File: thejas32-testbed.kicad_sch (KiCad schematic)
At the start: 128 parts, among them J1 Conn_02x04_Odd_Even, J10 Conn_02x10_Odd_Even, J11 Conn_02x03_Odd_Even, J13 Conn_02x06_Odd_Even, J15 Conn_01x04, J2 USB_B_Micro, J3 Conn_02x03_Odd_Even, J4 Conn_02x04_Odd_Even, J5 Conn_02x06_Odd_Even, J6 Conn_02x06_Odd_Even, J7 Conn_02x03_Odd_Even, J8 Conn_02x06_Odd_Even, J9 Conn_02x10_Odd_Even, U1 Pico Master, U2 THEJAS32, U3 Pico Slave, U4 MINI360 DC-DC, U5 MINI360 DC-DC, U6 W25Q16JVSSIQ

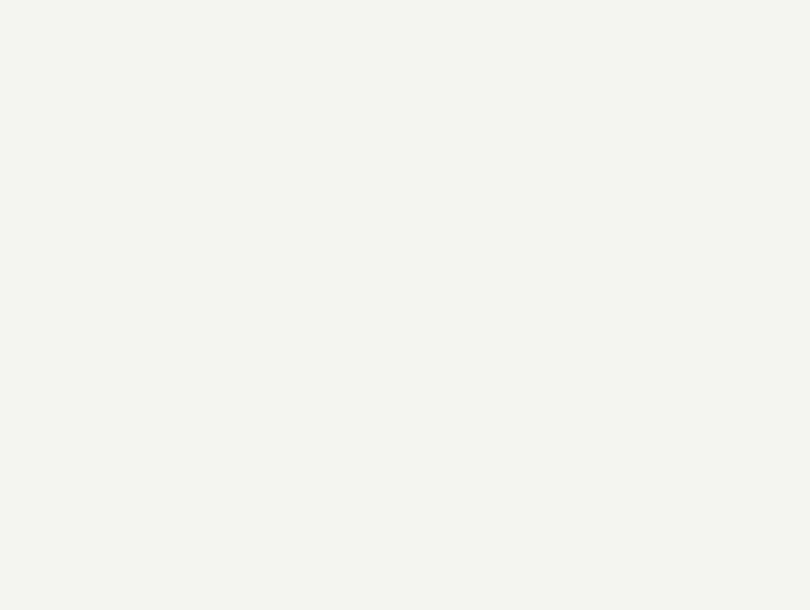
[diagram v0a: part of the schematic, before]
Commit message: Add PTH on board edges
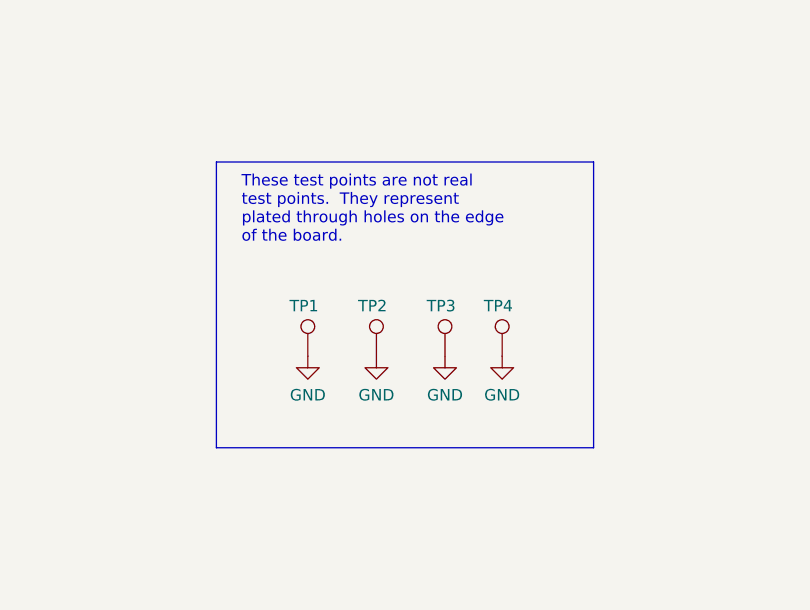
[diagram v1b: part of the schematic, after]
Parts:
- added TP1, TP2, TP3, TP4: Mounting Hole, MountingHole:MountingHole_3.2mm_M3_Pad, symbol Connector:TestPoint
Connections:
- net GND: now also TP1.1, TP2.1, TP3.1, TP4.1
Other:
- note added: "These test points are not real test points. They represent plated through holes on the edge of the board."

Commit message: Add footprint for Mini360
Roughly tested using calipers against a physical module.

Source of footprint:

https://github.com/rayvburn/KiCad/tree/master/Mini360_step_down_converter/Mini360_step-down.pretty

Commit 69583e8
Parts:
- U4, U5: footprint Module_DCDC:Mini 360 -> project_lib:Mini360_step-down
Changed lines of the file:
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@@
 			)
 		)
-		(property "Footprint" "Module_DCDC:Mini 360"
+		(property "Footprint" "project_lib:Mini360_step-down"
 			(at 252.73 128.27 0)
 			(effects
@@
 			)
 		)
-		(property "Footprint" "Module_DCDC:Mini 360"
+		(property "Footprint" "project_lib:Mini360_step-down"
 			(at 252.73 95.25 0)
 			(effects

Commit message: Various simplifications, initial routing.
This is a commit for review.

Schematic is modified to remove many zero ohms. RPi
connector brought in.

Layout shows 3V3 and 1V2 power planes. Pin mapping
may need to change to avoid usage of layer 3 for
signals if possible.
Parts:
- removed J15: Conn_01x04, Connector_PinHeader_2.54mm:PinHeader_1x04_P2.54mm_Vertical, symbol Connector_Generic:Conn_01x04
- removed J5, J8: Conn_02x06_Odd_Even, Connector_PinHeader_2.54mm:PinHeader_2x06_P2.54mm_Vertical, symbol Connector_Generic:Conn_02x06_Odd_Even
- removed J7: Conn_02x03_Odd_Even, Connector_PinHeader_2.54mm:PinHeader_2x03_P2.54mm_Vertical, symbol Connector_Generic:Conn_02x03_Odd_Even
- removed J9: Conn_02x10_Odd_Even, Connector_PinHeader_2.54mm:PinHeader_2x10_P2.54mm_Vertical, symbol Connector_Generic:Conn_02x10_Odd_Even
- removed R17, R19, R21, R23, R44, R45, R46, R47, R48, R49, R50, R51, R52, R53, R54, R55, R56, R57, R58, R59, R60, R61, R62, R63, R64, R65, R66, R67, R68, R69, R71: 0E, project_lib:proj_R_0603_1608Metric_Pad0.98x0.95mm_HandSolder, symbol Project-Specific:R_HandSolderable
- removed U4, U5: MINI360 DC-DC, project_lib:Mini360_step-down, symbol Mini360_Buck_Module:Mini360
- added J12: Conn_02x20_Odd_Even, Connector_PinHeader_2.54mm:PinHeader_2x20_P2.54mm_Vertical, symbol Connector_Generic:Conn_02x20_Odd_Even
- added J7: Conn_01x06, Connector_PinHeader_2.54mm:PinHeader_1x06_P2.54mm_Vertical, symbol Connector_Generic:Conn_01x06
- added JP1, JP2, JP3, JP4: Jumper_2_Bridged, Connector_PinHeader_2.54mm:PinHeader_1x02_P2.54mm_Vertical, symbol Jumper:Jumper_2_Bridged
- added U4, U5: ~, project_lib:Mini360_step-down, symbol Project-Specific:MINI360_DC-DC
- R38, R39, R40, R41, R42, R43: value 0E -> 10K
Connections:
- net +3V3 is gone; now on net PWR_3V3: C25.1, C25A1.1, J10.1 (Pin_1), J10.2 (Pin_2), J13.1 (Pin_1), J13.2 (Pin_2), J6.1 (Pin_1), J6.2 (Pin_2), U6.8 (VCC)
- net MCU_GPIO_02 is gone; now on net MCU_TST_CLK: R38.2
- net MCU_GPIO_03 is gone; now on net MCU_TJTAG_TMS: R39.2
- net MCU_GPIO_04 is gone; now on net MCU_TJTAG_TDI: R40.2
- net MCU_GPIO_05 is gone; now on net MCU_TJTAG_TCK: R41.2
- net MCU_GPIO_06 is gone; now on net MCU_TJTAG_TRST: R42.2
- net MCU_GPIO_07 is gone; now on net MCU_TST_MODE: R43.2
- net GND: now also R38.1, R39.1, R40.1, R41.1, R42.1, R43.1, J12.14 (Pin_14), J12.20 (Pin_20), J12.25 (Pin_25), J12.30 (Pin_30), J12.34 (Pin_34), J12.39 (Pin_39), J12.6 (Pin_6), J12.9 (Pin_9), J7.6 (Pin_6), U4.1 (IN-), U4.3 (OUT-), U5.1 (IN-), U5.3 (OUT-)
- net MCU_GPIO_16: now also U2.6 (GPIO16)
- net MCU_GPIO_17: now also U2.5 (GPIO17)
- net MCU_GPIO_18: now also U2.2 (GPIO18)
- net MCU_GPIO_19: now also U2.1 (GPIO19)
- net MCU_GPIO_20: now also U2.128 (GPIO20)
- net MCU_GPIO_21: now also U2.127 (GPIO21)
- net MCU_GPIO_22: now also U2.122 (GPIO22)
- net MCU_GPIO_23: now also U2.121 (GPIO23)
- net MCU_GPIO_24: now also U2.120 (GPIO24)
- net MCU_GPIO_25: now also U2.119 (GPIO25)
- net MCU_GPIO_26: now also U2.118 (GPIO26)
- net MCU_GPIO_27: now also U2.117 (GPIO27)
- net MCU_GPIO_28: now also U2.116 (GPIO28)
- net MCU_GPIO_29: now also U2.111 (GPIO29)
- net MCU_GPIO_30: now also U2.110 (GPIO30)
- net MCU_GPIO_31: now also U2.109 (GPIO31)
- net MCU_PWM_4: now also J7.2 (Pin_2)
- net MCU_PWM_5: now also J7.3 (Pin_3)
- net MCU_PWM_6: now also J7.4 (Pin_4)
- net MCU_PWM_7: now also J7.5 (Pin_5)
- net MCU_UART1_RX: now also U3.6 (GPIO4)
- net MCU_UART1_TX: now also U3.7 (GPIO5)
- net PWR_1V2: now also JP2.2 (B)
- net PWR_3V3: now also J12.1 (Pin_1), J12.17 (Pin_17), J7.1 (Pin_1), JP1.2 (B)
- net RPi_COMPAT_UART_TXD: now reaches R14.2
- net RPi_COMPAT_UART_TXD: now also J12.8 (Pin_8)
- net RPi_COMPAT_UART_RXD: now reaches R15.2
- net RPi_COMPAT_UART_RXD: now also J12.10 (Pin_10)
- net RPi_COMPAT_GPIO_7: now reaches U2.55 (GPIO11)
- net RPi_COMPAT_GPIO_7: now also J12.26 (Pin_26)
- net at U2.10 (SPI3_MISO): now also U6.2 (DO(IO1))
- net at U2.12 (SPI3_SS): now also U6.1 (~{CS})
- net MCU_TST_CLK: now reaches U2.20 (TST_CLK)
- net MCU_TJTAG_TMS: now reaches U2.22 (TJTAG_TMS)
- net MCU_TJTAG_TDI: now reaches U2.23 (TJTAG_TDI)
- net MCU_TJTAG_TCK: now reaches U2.28 (TJTAG_TCK)
- net MCU_TJTAG_TRST: now reaches U2.29 (TJTAG_TRST)
- net MCU_TST_MODE: now reaches U2.30 (TST_MODE)
- net RPi_COMPAT_I2C1_SCL: now reaches R4.2, U2.33 (I2C0_SCL)
- net RPi_COMPAT_I2C1_SCL: now also J12.5 (Pin_5)
- net RPi_COMPAT_I2C1_SDA: now reaches R5.2, U2.34 (I2C0_SDA)
- net RPi_COMPAT_I2C1_SDA: now also J12.3 (Pin_3)
- net at U2.39 (SPI1_SS): now also J13.5 (Pin_5)
- net at U2.41 (SPI1_MISO): now also J13.9 (Pin_9)
- net RPi_COMPAT_GPIO_21: now reaches U2.51 (GPIO15)
- net RPi_COMPAT_GPIO_21: now also J12.40 (Pin_40)
- net RPi_COMPAT_GPIO_20: now reaches U2.52 (GPIO14)
- net RPi_COMPAT_GPIO_20: now also J12.38 (Pin_38)
- net RPi_COMPAT_GPIO_16: now reaches U2.53 (GPIO13)
- net RPi_COMPAT_GPIO_16: now also J12.36 (Pin_36)
- net RPi_COMPAT_GPIO_1: now reaches U2.54 (GPIO12)
- net RPi_COMPAT_GPIO_1: now also J12.28 (Pin_28)
- net RPi_COMPAT_GPIO_25: now reaches U2.58 (GPIO10)
- net RPi_COMPAT_GPIO_25: now also J12.22 (Pin_22)
- net RPi_COMPAT_GPIO_24: now reaches U2.61 (GPIO9)
- net RPi_COMPAT_GPIO_24: now also J12.18 (Pin_18)
- net RPi_COMPAT_GPIO_23: now reaches U2.62 (GPIO8)
- net RPi_COMPAT_GPIO_23: now also J12.16 (Pin_16)
- net RPi_COMPAT_GPIO_4: now reaches U2.63 (GPIO7)
- net RPi_COMPAT_GPIO_4: now also J12.7 (Pin_7); no longer R43.1
- net RPi_COMPAT_GPIO_17: now reaches U2.64 (GPIO6)
- net RPi_COMPAT_GPIO_17: now also J12.11 (Pin_11); no longer R42.1
- net RPi_COMPAT_GPIO_27: now reaches U2.65 (GPIO5)
- net RPi_COMPAT_GPIO_27: now also J12.13 (Pin_13); no longer R41.1
- net RPi_COMPAT_GPIO_22: now reaches U2.66 (GPIO4)
- net RPi_COMPAT_GPIO_22: now also J12.15 (Pin_15); no longer R40.1
- net at U2.7 (SPI3_MOSI): now also U6.5 (DI(IO0))
- net RPi_COMPAT_GPIO_0: now reaches U2.71 (GPIO3)
- net RPi_COMPAT_GPIO_0: now also J12.27 (Pin_27); no longer R39.1
- net RPi_COMPAT_GPIO_5: now reaches U2.72 (GPIO2)
- net RPi_COMPAT_GPIO_5: now also J12.29 (Pin_29); no longer R38.1
- net RPi_COMPAT_SPI0_MISO: now reaches U2.90 (SPI0_MISO)
- net RPi_COMPAT_SPI0_MISO: now also J12.21 (Pin_21)
- net RPi_COMPAT_SPI0_CE0: now reaches U2.92 (SPI0_CSN)
- net RPi_COMPAT_SPI0_CE0: now also J12.24 (Pin_24)
- net PWR_5V: now reaches J2.1 (VBUS)
- net PWR_5V: now also J12.2 (Pin_2), J12.4 (Pin_4), JP3.1 (A), JP4.1 (A), U4.2 (IN+), U5.2 (IN+)
- net RPi_COMPAT_SPI0_MOSI: now reaches R18.2
- net RPi_COMPAT_SPI0_MOSI: now also J12.19 (Pin_19)
- net at U1.40 (VBUS): now also JP3.2 (B)
- net at U3.40 (VBUS): now also JP4.2 (B)
- net RPi_COMPAT_SPI0_SCLK: now reaches R16.2
- net RPi_COMPAT_SPI0_SCLK: now also J12.23 (Pin_23)
- net MCU_GPIO_00: no longer names the net of U1.4 (GPIO2)
- net MCU_GPIO_00: no longer R36.2
- net MCU_GPIO_01: no longer names the net of U1.5 (GPIO3)
- net MCU_GPIO_01: no longer R37.2
- net MCU_PWM_0 renamed RPi_COMPAT_PWM1
- net RPi_COMPAT_PWM1: now also J12.33 (Pin_33)
- net MCU_PWM_1 renamed RPi_COMPAT_PWM1_ALT
- net RPi_COMPAT_PWM1_ALT: now also J12.35 (Pin_35)
- net MCU_PWM_2 renamed RPi_COMPAT_PWM0
- net RPi_COMPAT_PWM0: now also J12.12 (Pin_12)
- net MCU_PWM_3 renamed RPi_COMPAT_PWM0_ALT
- net RPi_COMPAT_PWM0_ALT: now also J12.32 (Pin_32)
- new net: JP2.1 (A), U5.4 (OUT+)
- new net: JP1.1 (A), U4.4 (OUT+)
- new net RPi_COMPAT_GPIO_26: J12.37 (Pin_37), R36.2
- new net RPi_COMPAT_GPIO_6: J12.31 (Pin_31), R37.2
- no-connect marks 0 -> 48
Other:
- note added: "I2C0 is available on RPI header"
- note added: "Measure 1V2 power consumption in series here."
- note added: "Measure 3V3 power consumption in series here."
- note added: "PWR_FLAG eliminates false ERC errors due to jumpers"
- note added: "Populate this jumper to get power from main connector. Has benefits, including powering RP2040 for USB host."
- note added: "Populate this to get power from main connector. Has benefits, including powering RP2040 for USB host."
- note added: "Raspberry Pi Compatibility Header This header is to help plug common hats and get them to work. From a pinmux and functionality perspective, thejas32 doesn't match the RPi so it's a no-brainer that you should expect only some useful compatibility. Bear in mind that thejas pins have single functionality. E.g. UART pins can't be used as GPIOs... The following are ensured: 3.3V, 5V for appropriately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"
- note added: "SPI0 is available on RPI header"
- note added: "UART2 goes to RPi Connector"
- note removed: "GPIO Header 2"
- note removed: "I2C0 can be tapped here"
- moved on the sheet: C1, C1A1, C2, C2A1, C3, C3A1

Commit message: Review,power shapes,dcap placement from Atharva
All dcaps are now at layer 4, leaving lot
more space on layer 1 for signal breakout.

Flow of 1V2 power is deemed good - power plane,
flowing to caps, through via to pins. Flow of 3V3
power is reasonable - power plane with vias to both
caps and pins.

Connectors and component placements need to be
finalized next, and routed.
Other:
- note added: "Aligned Mounting holes"
- note added: "Change R2 to 100k for weak PD"
- note added: "Change R3 to 100k for weak PD"
- note added: "DEbug UART 0 for master Pico is not conneted anywhere"
- note added: "Need to add Properties like MPN Manufacturer in properties for easier BOM creation"
- note added: "Need to check of R4/R5 has any PU for I2C on Main RasPi. If there, remove R4/R5"
- note added: "When Powering through RasPi, remove JP1"
- moved on the sheet: C11A1
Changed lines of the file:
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@@
 	)
 	(junction
-		(at 314.96 240.03)
-		(diameter 0)
-		(color 0 0 0 0)
-	)
-	(junction
 		(at 175.26 349.25)
 		(diameter 0)
@@
 	)
 	(junction
-		(at 325.12 240.03)
-		(diameter 0)
-		(color 0 0 0 0)
-	)
-	(junction
 		(at 233.68 233.68)
 		(diameter 0)
@@
 	)
 	(junction
-		(at 304.8 240.03)
-		(diameter 0)
-		(color 0 0 0 0)
-	)
-	(junction
 		(at 368.3 393.7)
 		(diameter 0)
@@
 	)
 	(junction
-		(at 335.28 240.03)
-		(diameter 0)
-		(color 0 0 0 0)
-	)
-	(junction
 		(at 58.42 220.98)
 		(diameter 0)
@@
 	)
 	(junction
-		(at 295.91 240.03)
-		(diameter 0)
-		(color 0 0 0 0)
-	)
-	(junction
 		(at 304.8 229.87)
 		(diameter 0)
@@
 	)
 	(junction
-		(at 285.75 240.03)
-		(diameter 0)
-		(color 0 0 0 0)
-	)
-	(junction
 		(at 273.05 284.48)
 		(diameter 0)
@@
 	(wire
 		(pts
-			(xy 314.96 237.49) (xy 314.96 240.03)
+			(xy 314.96 238.76) (xy 314.96 240.03)
 		)
 		(stroke
@@
 	(wire
 		(pts
+			(xy 314.96 231.14) (xy 314.96 229.87)
+		)
+		(stroke
+			(width 0)
+			(type default)
+		)
+	)
+	(wire
+		(pts
 			(xy 74.93 281.94) (xy 149.86 281.94)
 		)
@@
 	(wire
 		(pts
-			(xy 285.75 240.03) (xy 285.75 241.3)
-		)
-		(stroke
-			(width 0)
-			(type default)
-		)
-	)
-	(wire
-		(pts
 			(xy 755.65 424.18) (xy 755.65 440.69)
 		)
@@
 	(wire
 		(pts
-			(xy 335.28 240.03) (xy 335.28 241.3)
-		)
-		(stroke
-			(width 0)
-			(type default)
-		)
-	)
-	(wire
-		(pts
 			(xy 99.06 349.25) (xy 99.06 351.79)
 		)
@@
 	(wire
 		(pts
-			(xy 304.8 240.03) (xy 304.8 241.3)
-		)
-		(stroke
-			(width 0)
-			(type default)
-		)
-	)
-	(wire
-		(pts
 			(xy 130.81 309.88) (xy 149.86 309.88)
 		)
@@
 	(wire
 		(pts
-			(xy 314.96 240.03) (xy 314.96 241.3)
-		)
-		(stroke
-			(width 0)
-			(type default)
-		)
-	)
-	(wire
-		(pts
 			(xy 701.04 473.71) (xy 701.04 486.41)
 		)
@@
 	(wire
 		(pts
-			(xy 295.91 240.03) (xy 295.91 241.3)
-		)
-		(stroke
-			(width 0)
-			(type default)
-		)
-	)
-	(wire
-		(pts
 			(xy 444.5 337.82) (xy 453.39 337.82)
 		)
@@
 	(wire
 		(pts
-			(xy 325.12 240.03) (xy 325.12 241.3)
-		)
-		(stroke
-			(width 0)
-			(type default)
-		)
-	)
-	(wire
-		(pts
 			(xy 118.11 396.24) (xy 118.11 400.05)
 		)
@@
 		)
 	)
+	(text "Aligned Mounting holes"
+		(exclude_from_sim no)
+		(at 744.474 64.516 0)
+		(effects
+			(font
+				(size 1.27 1.27)
+				(color 255 30 34 1)
+			)
+			(justify left bottom)
+		)
+	)
 	(text "I2C0 is available \non RPI header"
 		(exclude_from_sim no)
@@
 		)
 	)
+	(text "Need to check of R4/R5 has any PU for I2C on Main RasPi. \nIf there, remove R4/R5"
+		(exclude_from_sim no)
+		(at 744.982 36.322 0)
+		(effects
+			(font
+				(size 1.27 1.27)
+				(color 255 30 34 1)
+			)
+			(justify left bottom)
+		)
+	)
 	(text "Order of Pins:\nGND,\nCLK, CSN, MOSI, MISO\nVCC"
 		(exclude_from_sim no)
@@
 		)
 	)
+	(text "When Powering through RasPi, remove JP1"
+		(exclude_from_sim no)
+		(at 268.986 109.22 0)
+		(effects
+			(font
+				(size 1.27 1.27)
+				(color 255 30 34 1)
+			)
+			(justify left bottom)
+		)
+	)
 	(text "SPI2 bus"
 		(exclude_from_sim no)
@@
 		)
 	)
+	(text "When Powering through RasPi, remove JP1"
+		(exclude_from_sim no)
+		(at 744.982 44.958 0)
+		(effects
+			(font
+				(size 1.27 1.27)
+				(color 255 30 34 1)
+			)
+			(justify left bottom)
+		)
+	)
 	(text "spi1\nslave interface"
 		(exclude_from_sim no)
@@
 		)
 	)
+	(text "Change R2 to 100k for weak PD\n"
+		(exclude_from_sim no)
+		(at 744.728 26.924 0)
+		(effects
+			(font
+				(size 1.27 1.27)
+				(color 255 30 34 1)
+			)
+			(justify left bottom)
+		)
+	)
 	(text "PWR_FLAG eliminates\nfalse ERC errors due\nto jumpers"
 		(exclude_from_sim no)
@@
 		)
 	)
+	(text "Need to add Properties like\nMPN\nManufacturer \nin properties for easier BOM creation"
+		(exclude_from_sim no)
+		(at 744.982 22.352 0)
+		(effects
+			(font
+				(size 1.27 1.27)
+				(color 255 30 34 1)
+			)
+			(justify left bottom)
+		)
+	)
 	(text "See layout instructions for decaps"
 		(exclude_from_sim no)
@@
 		)
 	)
+	(text "DEbug UART 0 for master Pico is not conneted anywhere"
+		(exclude_from_sim no)
+		(at 744.982 41.148 0)
+		(effects
+			(font
+				(size 1.27 1.27)
+				(color 255 30 34 1)
+			)
+			(justify left bottom)
+		)
+	)
 	(text "See layout instructions for decaps"
 		(exclude_from_sim no)
@@
 		)
 	)
+	(text "Change R3 to 100k for weak PD\n"
+		(exclude_from_sim no)
+		(at 744.982 30.734 0)
+		(effects
+			(font
+				(size 1.27 1.27)
+				(color 255 30 34 1)
+			)
+			(justify left bottom)
+		)
+	)
 	(global_label "MCU_TST_MODE"
 		(shape input)
@@
 		)
 		(property "Value" "GND"
-			(at 314.96 244.348 0)
+			(at 314.96 246.888 0)
 			(effects
 				(font
 					(size 1.27 1.27)
 				)
+				(hide yes)
 			)
 		)
@@
 		)
 		(property "Value" "GND"
-			(at 295.91 244.348 0)
+			(at 295.91 246.888 0)
 			(effects
 				(font
 					(size 1.27 1.27)
 				)
+				(hide yes)
 			)
 		)
@@
 		)
 		(property "Value" "GND"
-			(at 304.8 244.348 0)
+			(at 304.8 246.888 0)
 			(effects
 				(font
 					(size 1.27 1.27)
 				)
+				(hide yes)
 			)
 		)
@@
 	(symbol
 		(lib_id "Project-Specific:DCAP_Farther")
-		(at 314.96 233.68 0)
+		(at 314.96 234.95 0)
 		(unit 1)
 		(exclude_from_sim no)
@@
 		(dnp no)
 		(property "Reference" "C11A1"
-			(at 316.23 237.236 0)
+			(at 316.23 238.506 0)
 			(effects
 				(font
@@
 		)
 		(property "Value" "10uF"
-			(at 316.23 239.776 0)
+			(at 316.23 241.046 0)
 			(effects
 				(font
@@
 		)
 		(property "Footprint" "project_lib:proj_C_0603_1608Metric_Pad1.08x0.95mm_HandSolder"
-			(at 315.9252 237.49 0)
+			(at 315.9252 238.76 0)
 			(effects
 				(font
@@
 		)
 		(property "Datasheet" "~"
-			(at 314.96 233.68 0)
+			(at 314.96 234.95 0)
 			(effects
 				(font
@@
 		)
 		(property "Description" "Decoupling Capacitor farther from power pin"
-			(at 314.96 233.68 0)
+			(at 314.96 234.95 0)
 			(effects
 				(font
@@
 		)
 		(property "Value" "GND"
-			(at 335.28 244.348 0)
+			(at 335.28 246.888 0)
 			(effects
 				(font
 					(size 1.27 1.27)
 				)
+				(hide yes)
 			)
 		)
@@
 		)
 		(property "Value" "GND"
-			(at 325.12 244.348 0)
+			(at 325.12 246.888 0)
 			(effects
 				(font
 					(size 1.27 1.27)
 				)
+				(hide yes)
 			)
 		)
@@
 		)
 		(property "Value" "GND"
-			(at 285.75 244.348 0)
+			(at 285.75 246.888 0)
 			(effects
 				(font
 					(size 1.27 1.27)
 				)
+				(hide yes)
 			)
 		)

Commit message: Remap pins for less criss cross. Get rid of tracks
Got rid of tracks to start tracks afresh once placement is
done.
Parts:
- removed R10, R11, R14, R15: 0E, project_lib:proj_R_0603_1608Metric_Pad0.98x0.95mm_HandSolder, symbol Project-Specific:R_HandSolderable
- added TP5, TP6: Mounting Hole, MountingHole:MountingHole_3.2mm_M3_Pad, symbol Connector:TestPoint
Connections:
- net GND: now also TP5.1, TP6.1
- net MCU_GPIO_16: now also J10.4 (Pin_4); no longer J10.3 (Pin_3)
- net MCU_GPIO_17: now also J10.3 (Pin_3); no longer J10.5 (Pin_5)
- net MCU_GPIO_18: now also J10.6 (Pin_6); no longer J10.7 (Pin_7)
- net MCU_GPIO_19: now also J10.5 (Pin_5); no longer J10.9 (Pin_9)
- net MCU_GPIO_20: now also J10.8 (Pin_8); no longer J10.11 (Pin_11)
- net MCU_GPIO_21: now also J10.7 (Pin_7); no longer J10.13 (Pin_13)
- net MCU_GPIO_22: now also J10.10 (Pin_10); no longer J10.15 (Pin_15)
- net MCU_GPIO_23: now also J10.9 (Pin_9); no longer J10.17 (Pin_17)
- net MCU_GPIO_24: now also J10.12 (Pin_12); no longer J10.4 (Pin_4)
- net MCU_GPIO_25: now also J10.11 (Pin_11); no longer J10.6 (Pin_6)
- net MCU_GPIO_26: now also J10.14 (Pin_14); no longer J10.8 (Pin_8)
- net MCU_GPIO_27: now also J10.13 (Pin_13); no longer J10.10 (Pin_10)
- net MCU_GPIO_28: now also J10.16 (Pin_16); no longer J10.12 (Pin_12)
- net MCU_GPIO_29: now also J10.15 (Pin_15); no longer J10.14 (Pin_14)
- net MCU_GPIO_30: now also J10.18 (Pin_18); no longer J10.16 (Pin_16)
- net MCU_GPIO_31: now also J10.17 (Pin_17); no longer J10.18 (Pin_18)
- net MCU_I2C1_SCL: now also U3.9 (GPIO6); no longer U1.9 (GPIO6)
- net MCU_I2C1_SDA: now also U3.10 (GPIO7); no longer U1.10 (GPIO7)
- net RPi_COMPAT_GPIO_0: now also U2.61 (GPIO9); no longer U2.71 (GPIO3)
- net RPi_COMPAT_GPIO_1: now also U2.62 (GPIO8); no longer U2.54 (GPIO12)
- net RPi_COMPAT_GPIO_16: now also U2.54 (GPIO12); no longer U2.53 (GPIO13)
- net RPi_COMPAT_GPIO_17: now also R37.2; no longer U2.64 (GPIO6)
- net RPi_COMPAT_GPIO_23: now also U2.71 (GPIO3); no longer U2.62 (GPIO8)
- net RPi_COMPAT_GPIO_24: now also U2.65 (GPIO5); no longer U2.61 (GPIO9)
- net RPi_COMPAT_GPIO_25: now also U2.64 (GPIO6); no longer U2.58 (GPIO10)
- net RPi_COMPAT_GPIO_26: now also U2.53 (GPIO13); no longer R36.2
- net RPi_COMPAT_GPIO_27: now also U2.72 (GPIO2); no longer U2.65 (GPIO5)
- net RPi_COMPAT_GPIO_4: now also R36.2; no longer U2.63 (GPIO7)
- net RPi_COMPAT_GPIO_5: now also U2.58 (GPIO10); no longer U2.72 (GPIO2)
- net RPi_COMPAT_GPIO_6: now also U2.55 (GPIO11); no longer R37.2
- net RPi_COMPAT_GPIO_7: now also U2.63 (GPIO7); no longer U2.55 (GPIO11)
- net RPi_COMPAT_I2C1_SCL: now also R8.2, U2.32 (I2C2_SCL); no longer R4.2, U2.33 (I2C0_SCL)
- net RPi_COMPAT_I2C1_SDA: now also R9.2, U2.31 (I2C2_SDA); no longer R5.2, U2.34 (I2C0_SDA)
- net RPi_COMPAT_SPI0_CE0: now also R25.2; no longer U2.92 (SPI0_CSN)
- net RPi_COMPAT_SPI0_MISO: now also R27.2; no longer U2.90 (SPI0_MISO)
- net RPi_COMPAT_SPI0_MOSI: now also R26.2; no longer R18.2
- net RPi_COMPAT_SPI0_SCLK: now also R24.2; no longer R16.2
- net RPi_COMPAT_UART_RXD: now also U2.105 (UART2_RX)
- net RPi_COMPAT_UART_TXD: now also U2.106 (UART2_TX)
- net at U2.107 (UART0_RX): now also J3.3 (Pin_3)
- net at U2.108 (UART0_TX): now also J3.1 (Pin_1)
- net at J6.5 (Pin_5): now also U2.92 (SPI0_CSN); no longer R25.2
- net at J6.9 (Pin_9): now also U2.90 (SPI0_MISO); no longer R27.2
- net at J6.3 (Pin_3): now also R16.2; no longer R24.2
- net at J6.7 (Pin_7): now also R18.2; no longer R26.2
- net MCU_I2C2_SCL renamed MCU_I2C0_SCL
- net MCU_I2C0_SCL: now also J4.6 (Pin_6), U1.10 (GPIO7), U1.9 (GPIO6); no longer U3.9 (GPIO6)
- removed net MCU_I2C2_SDA: J4.6 (Pin_6), U3.10 (GPIO7)
- net MCU_SPI2_CSN renamed MCU_SPI0_CSN
- net MCU_SPI2_MISO renamed MCU_SPI0_MISO
- net MCU_SPI2_MOSI renamed MCU_SPI0_MOSI
- net MCU_SPI2_SCK renamed MCU_SPI0_SCK
- new net: J4.3 (Pin_3), R4.2, U2.33 (I2C0_SCL)
- new net: J4.5 (Pin_5), R5.2, U2.34 (I2C0_SDA)
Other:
- note added: "SPI2 is available on RPI header"
- note removed: "SPI0 is available on RPI header"
- moved on the sheet: J6, R4, R5

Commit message: Reduce criss cross further with mapping changes
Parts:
- removed J7: Conn_01x06, Connector_PinHeader_2.54mm:PinHeader_1x06_P2.54mm_Vertical, symbol Connector_Generic:Conn_01x06
- removed R12, R13: 0E, project_lib:proj_R_0603_1608Metric_Pad0.98x0.95mm_HandSolder, symbol Project-Specific:R_HandSolderable
- added J7: Conn_01x05, Connector_PinHeader_2.54mm:PinHeader_1x05_P2.54mm_Vertical, symbol Connector_Generic:Conn_01x05
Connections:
- net GND: now also J7.5 (Pin_5)
- net MCU_I2C0_SCL: no longer J4.6 (Pin_6), U1.10 (GPIO7)
- net MCU_PWM_4: now also J7.2 (Pin_2)
- net MCU_PWM_5: now also J7.3 (Pin_3)
- net MCU_PWM_6: now also J7.4 (Pin_4)
- net MCU_RESETN: no longer U1.25 (GPIO19)
- net PWR_3V3: now also J7.1 (Pin_1)
- net RPi_COMPAT_GPIO_0: now also U2.62 (GPIO8); no longer U2.61 (GPIO9)
- net RPi_COMPAT_GPIO_1: now also U2.61 (GPIO9); no longer U2.62 (GPIO8)
- net RPi_COMPAT_GPIO_22: now also U2.71 (GPIO3); no longer U2.66 (GPIO4)
- net RPi_COMPAT_GPIO_23: now also U2.66 (GPIO4); no longer U2.71 (GPIO3)
- net at U2.45 (UART1_TX): now also J11.1 (Pin_1)
- net at U2.50 (UART1_RX): now also J11.3 (Pin_3)
- new net MCU_I2C0_SDA: J4.6 (Pin_6), U1.10 (GPIO7)
- no-connect marks 48 -> 50
